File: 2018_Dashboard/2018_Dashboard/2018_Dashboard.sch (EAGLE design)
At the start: 29 parts, among them U1 SN74HC595D, U2 ATMEGA328P_PDIP_EZ, U3 SN74HC595D

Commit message: Changed resistors from before seven segment to after seven segment, reduced number of resistors
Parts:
- removed DISP1: ATA8041AB, SparkFun-LED:7-SEGMENT-4DIGIT-20MM-BLUE
- removed R5, R6, R7: 330, SparkFun-Resistors:330OHM-0603-1/10W-1%
- removed U2: ATMEGA328P_PDIP_EZ, SparkFun-IC-Microcontroller:ATMEGA328P_PDIP_EZ
- added BLUE2, BLUE3, BLUE4, LED13: TLLG4400, led:TLLG4400
- added C1: 0.1uF, SparkFun-Capacitors:0.1UF-0603-25V-(+80/-20%)
- added C2, C3: 22pF, SparkFun-Capacitors:22PF-0603-50V-5%
- added C4, C5: 560pF, SparkFun-Capacitors:560PF-0603-50V-5%
- added CAN, POWER: (no value), SparkFun-Connectors:CONN_02
- added CANH, CANL: 100, SparkFun-Resistors:100OHM-0603-1/4W-5%
- added CAN_INTERFACE: MCP2551, SparkFun-IC-Comms:MCP2551
- added CAN_SERIAL: MCP2515, SparkFun-IC-Comms:MCP2515(MCP2510)SO
- added CONTROL: ATMEGA328P_TQFP, SparkFun-IC-Microcontroller:ATMEGA328P_TQFP
- added PROGRAM: 455-1750-1-ND, SparkFun-Connectors:CONN_03
- added R17, R18, R19, R20: 330, SparkFun-Resistors:330OHM-0603-1/10W-1%
- added R21: 10k, SparkFun-Resistors:10KOHM-0603-1/10W-1%
- added R22: 4.7k, SparkFun-Resistors:4.7KOHM-0603-1/10W-1%
- added SEVEN_SEGMENT: ATA8041AB, SparkFun-LED:7-SEGMENT-4DIGIT-20MM-BLUE
- added SHIFT_3: SN74HC595D, SparkFun-IC-Logic:74HC595D
- added Y1: 16MHz, SparkFun-Clocks:CRYSTAL-16MHZPTH-HC49US
- renumbered LED1 to GREEN1, LED2 to GREEN2, LED3 to GREEN3, LED4 to GREEN4, LED5 to RED1, LED6 to RED2, LED7 to RED3, LED8 to RED4, LED9 to BLUE1, U1 to SHIFT_1, U3 to SHIF_2
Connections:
- removed net N$38: BLUE1.C, GREEN1.C, GREEN2.C, GREEN3.C, GREEN4.C, RED1.C, RED2.C, RED3.C, RED4.C, SHIFT_1.GND, SHIF_2.GND, U2.GND@1, U2.GND@2
- removed net N$7: R5.2, SHIFT_1.QE
- removed net N$8: R6.2, SHIFT_1.QF
- removed net N$9: R7.2, SHIFT_1.QG
- new net CANH: CAN.2, CANH.1, CAN_INTERFACE.CANH
- new net CANL: CAN.1, CANL.1, CAN_INTERFACE.CANL
- new net GND: BLUE1.C, BLUE2.C, BLUE3.C, BLUE4.C, C1.2, C2.1, C3.1, C4.2, C5.2, CAN_INTERFACE.VSS, CONTROL.GND@3, CONTROL.GND@5, GREEN1.C, GREEN2.C, GREEN3.C, GREEN4.C, POWER.2, R22.1, RED1.C, RED2.C, RED3.C, RED4.C, SHIFT_1.GND, SHIFT_3.GND, SHIF_2.GND
- new net N$39: R9.1, SHIF_2.QE
- new net N$40: R10.1, SHIF_2.QF
- new net N$41: R11.1, SHIF_2.QG
- new net N$42: R12.1, SHIF_2.QH
- new net N$43: R13.1, SHIFT_3.QA
- new net N$44: R14.1, SHIFT_3.QB
- new net N$45: R15.1, SHIFT_3.QC
- new net N$46: R16.1, SHIFT_3.QD
- new net N$47: R2.1, SEVEN_SEGMENT.D2
- new net N$48: R3.1, SEVEN_SEGMENT.D3
- new net N$49: R4.1, SEVEN_SEGMENT.D4
- new net N$50: LED13.A, R20.1
- new net N$51: CONTROL.PC0(ADC0), LED13.C
- new net N$52: CAN_SERIAL>NAME.CS, CONTROL.PB2(SS/OC1B)
- new net N$53: CAN_SERIAL>NAME.SI, CONTROL.PB3(MOSI/OC2)
- new net N$54: CAN_SERIAL>NAME.SO, CONTROL.PB4(MISO)
- new net N$55: CAN_SERIAL>NAME.SCK, CONTROL.PB5(SCK)
- new net N$56: CAN_SERIAL>NAME.INT, CONTROL.PD2(INT0)
- new net N$57: CAN_INTERFACE.TXD, CAN_SERIAL>NAME.TXCAN
- new net N$58: CAN_INTERFACE.RXD, CAN_SERIAL>NAME.RXCAN
- new net N$59: C3.2, CAN_SERIAL>NAME.OSC2, Y1.1
- new net N$61: CAN_INTERFACE.RS, CAN_SERIAL>NAME.RESET, PROGRAM.3, R22.2
- new net N$62: C4.1, CANH.2
- new net N$63: C2.2, CAN_SERIAL>NAME.OSC1, Y1.2
- new net N$65: C5.1, CANL.2
- new net N$67: CONTROL.PD0(RXD), PROGRAM.1
- new net N$68: CONTROL.PD1(TXD), PROGRAM.2
- new net VCC: C1.1, CAN_INTERFACE.VDD, CONTROL.AVCC, CONTROL.VCC@4, CONTROL.VCC@6, POWER.1, R20.2, R21.1, SHIFT_1.SCL, SHIFT_1.VCC, SHIFT_3.SCL, SHIFT_3.VCC, SHIF_2.SCL, SHIF_2.VCC
- net N$1: now also CONTROL.PC6(/RESET), R21.2; no longer SHIFT_1.SCL, SHIFT_1.VCC, SHIF_2.SCL, SHIF_2.VCC, U2.VCC
- net N$10: now also SHIFT_3.SER, SHIF_2.QH*; no longer DISP1.A, R1.1
- net N$11: now also SEVEN_SEGMENT.A, SHIFT_1.QA; no longer DISP1.B, R2.1
- net N$12: now also SEVEN_SEGMENT.B, SHIFT_1.QB; no longer DISP1.C, R3.1
- net N$13: now also SEVEN_SEGMENT.C, SHIFT_1.QC; no longer DISP1.D, R4.1
- net N$14: now also SEVEN_SEGMENT.D, SHIFT_1.QD; no longer DISP1.E, R5.1
- net N$15: now also SEVEN_SEGMENT.E, SHIFT_1.QE; no longer DISP1.F, R6.1
- net N$16: now also SEVEN_SEGMENT.F, SHIFT_1.QF; no longer DISP1.G, R7.1
- net N$17: now also SEVEN_SEGMENT.G, SHIFT_1.QG; no longer R8.1, SHIF_2.QA
- net N$18: now also BLUE2.A, R17.2; no longer R9.1, SHIF_2.QB
- net N$19: now also BLUE3.A, R18.2; no longer R10.1, SHIF_2.QC
- net N$20: now also CONTROL.PD5(T1); no longer U2.PD5(T1)
- net N$21: now also CONTROL.PD6(AIN0), SHIFT_3.SCK; no longer U2.PD6(AIN0)
- net N$22: now also CONTROL.PD7(AIN1), SHIFT_3.RCK; no longer U2.PD7(AIN1)
- net N$23: now also BLUE4.A, R19.2; no longer R11.1, SHIF_2.QD
- net N$24: now also R1.1, SEVEN_SEGMENT.D1; no longer R12.1, SHIF_2.QE
- net N$25: now also R19.1, SHIF_2.QA; no longer R13.1, SHIF_2.QF
- net N$26: now also R18.1, SHIF_2.QB; no longer R14.1, SHIF_2.QG
- net N$27: now also R17.1, SHIF_2.QC; no longer R15.1, SHIF_2.QH
- net N$28: now also R8.1, SHIF_2.QD; no longer R16.1, SHIF_2.QH*
- net N$3: now also SHIFT_3.QE; no longer SHIFT_1.QA
- net N$4: now also SHIFT_3.QF; no longer SHIFT_1.QB
- net N$5: now also SHIFT_3.QG; no longer SHIFT_1.QC
- net N$6: now also SHIFT_3.QH; no longer SHIFT_1.QD
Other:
- moved on the sheet: R1, R2, R3, R4

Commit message: Added silkscreen stuff
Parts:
- renumbered BLUE1 to B1, BLUE2 to B2, BLUE3 to B3, BLUE4 to B4, GREEN1 to G1, GREEN2 to G2, GREEN3 to G3, GREEN4 to G4, LED13 to OVERHEAT, RED1 to RD1, RED2 to RD2, RED3 to RD3, RED4 to RD4

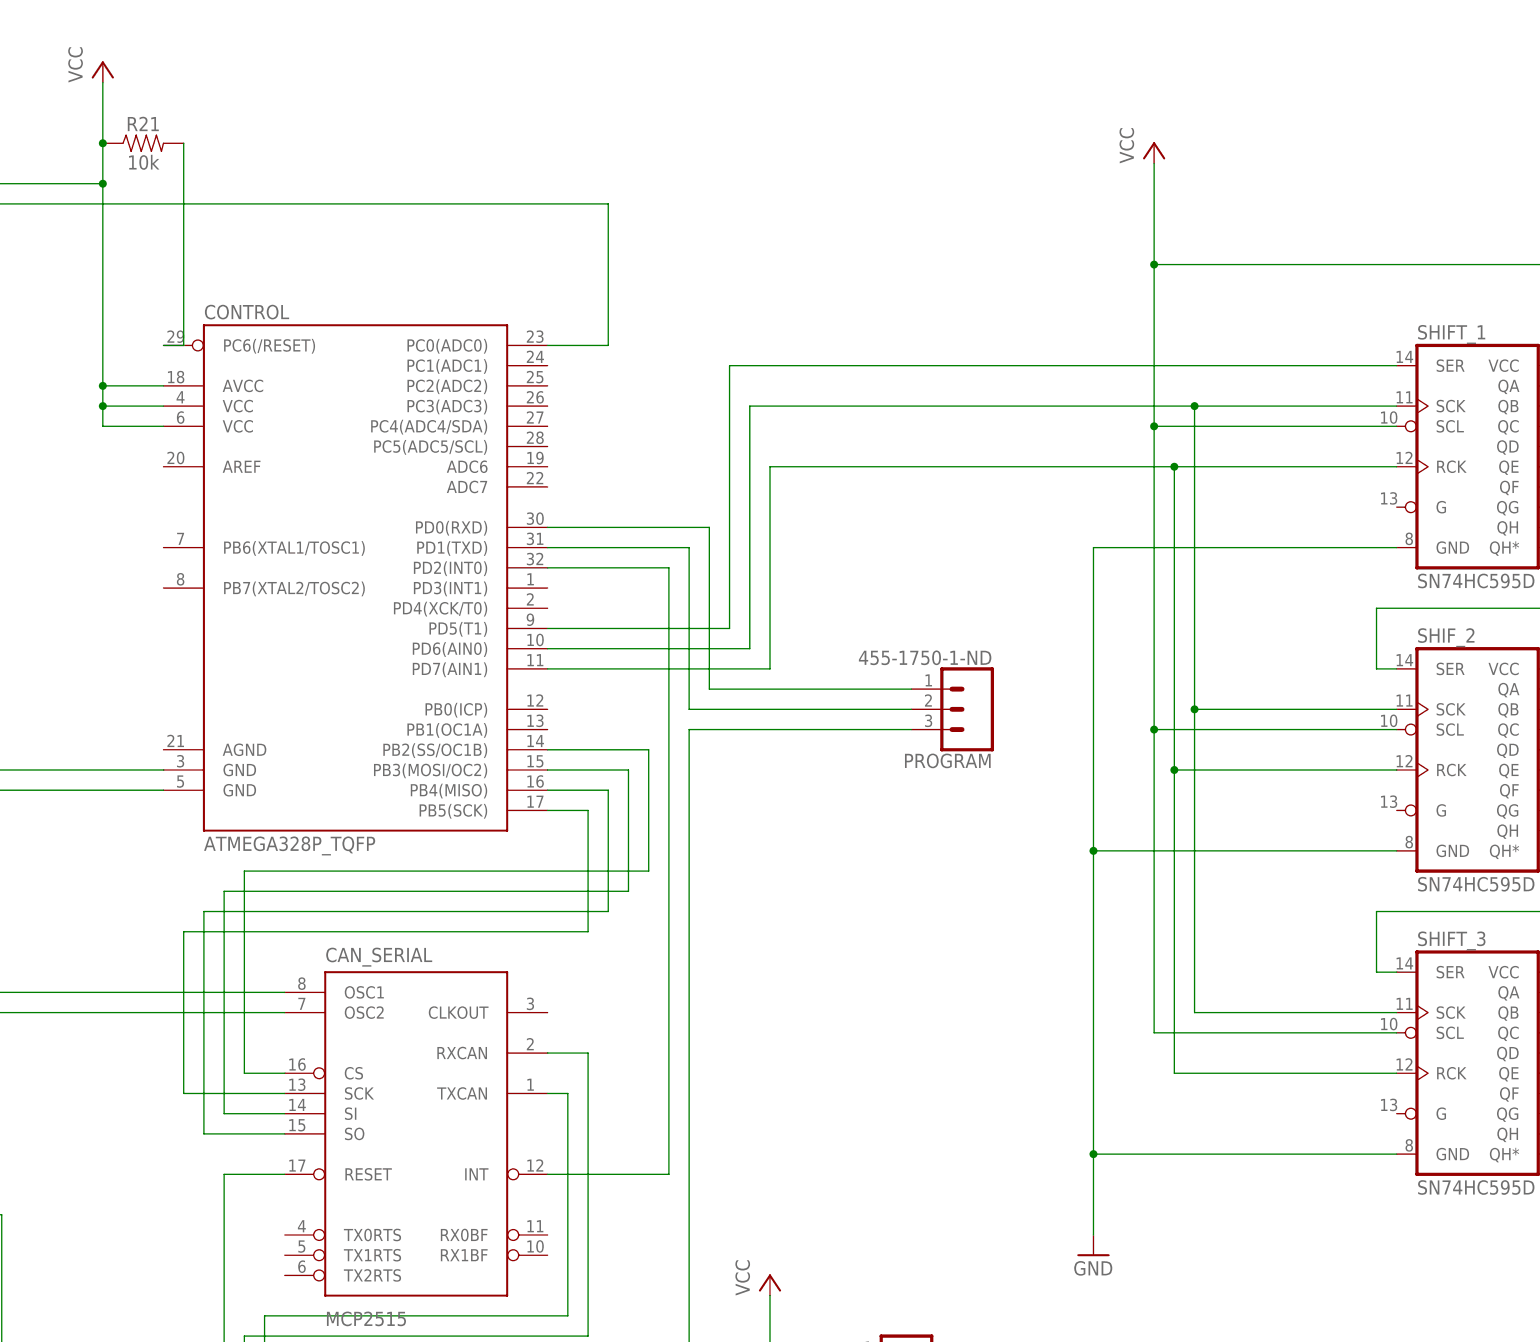
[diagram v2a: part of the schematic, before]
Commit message: fixed power net for can communication
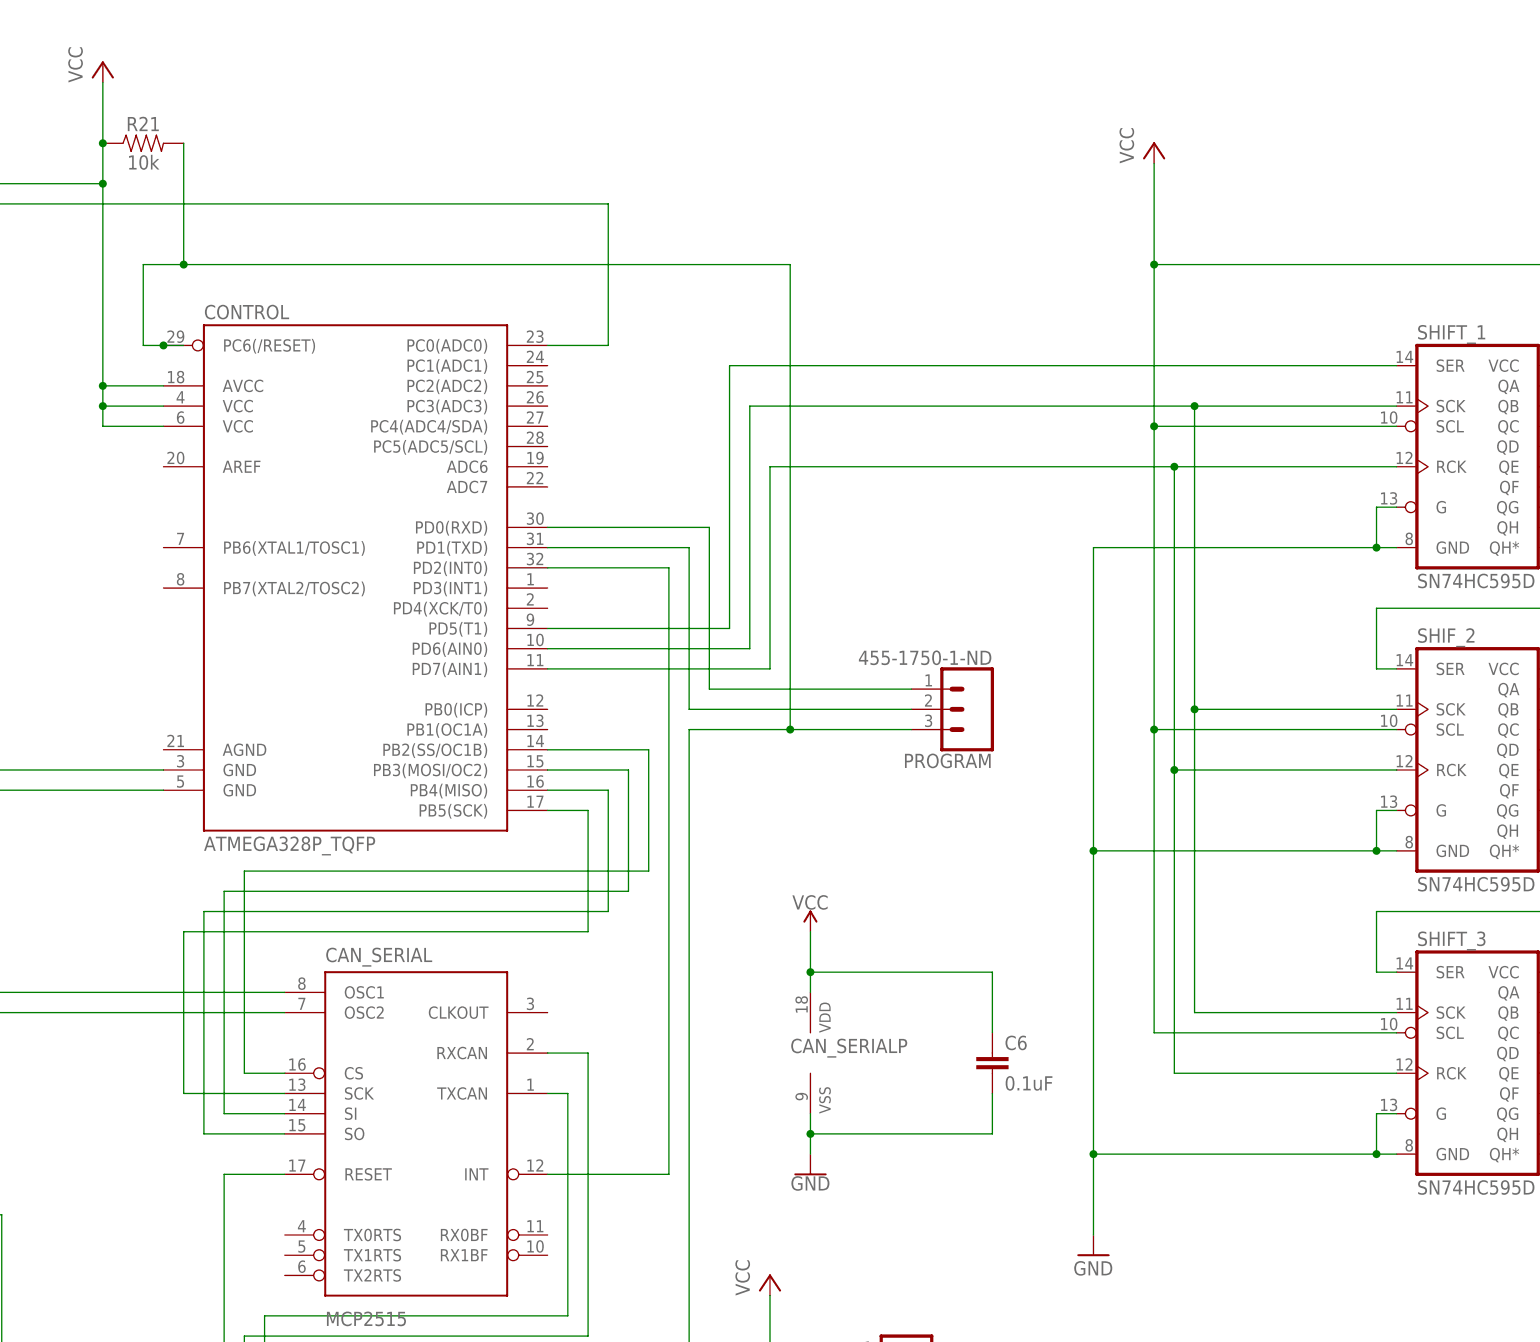
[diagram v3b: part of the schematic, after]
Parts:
- added C6: 0.1uF, SparkFun-Capacitors:0.1UF-0402-16V-10%
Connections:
- removed net N$1: CONTROL.PC6(/RESET), R21.2
- net GND: now also C6.2, CAN_SERIALP.VSS, SHIFT_1.G, SHIFT_3.G, SHIF_2.G
- net N$61: now also CONTROL.PC6(/RESET), R21.2
- net VCC: now also C6.1, CAN_SERIALP.VDD
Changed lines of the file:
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@@
 <part name="R3" library="SparkFun-Resistors" deviceset="330OHM" device="-0603-1/10W-1%" value="330"/>
 <part name="R4" library="SparkFun-Resistors" deviceset="330OHM" device="-0603-1/10W-1%" value="330"/>
+<part name="SUPPLY1" library="SparkFun-PowerSymbols" deviceset="VCC" device=""/>
+<part name="GND8" library="SparkFun-PowerSymbols" deviceset="GND" device=""/>
+<part name="C6" library="SparkFun-Capacitors" deviceset="0.1UF" device="-0402-16V-10%" value="0.1uF"/>
 </parts>
 <sheets>
@@
 <instance part="R3" gate="G$1" x="73.66" y="-50.8" rot="R90"/>
 <instance part="R4" gate="G$1" x="81.28" y="-50.8" rot="R90"/>
+<instance part="CAN_SERIAL" gate="P" x="-68.58" y="35.56"/>
+<instance part="SUPPLY1" gate="G$1" x="-68.58" y="50.8"/>
+<instance part="GND8" gate="1" x="-68.58" y="20.32"/>
+<instance part="C6" gate="G$1" x="-45.72" y="33.02"/>
 </instances>
 <busses>
@@
 <pinref part="SHIFT_3" gate="U1" pin="GND"/>
 <wire x1="-33.02" y1="12.7" x2="-33.02" y2="22.86" width="0.1524" layer="91"/>
-<wire x1="-33.02" y1="22.86" x2="5.08" y2="22.86" width="0.1524" layer="91"/>
+<wire x1="-33.02" y1="22.86" x2="2.54" y2="22.86" width="0.1524" layer="91"/>
 <pinref part="SHIF_2" gate="U1" pin="GND"/>
+<wire x1="2.54" y1="22.86" x2="5.08" y2="22.86" width="0.1524" layer="91"/>
 <wire x1="-33.02" y1="22.86" x2="-33.02" y2="60.96" width="0.1524" layer="91"/>
-<wire x1="-33.02" y1="60.96" x2="5.08" y2="60.96" width="0.1524" layer="91"/>
+<wire x1="-33.02" y1="60.96" x2="2.54" y2="60.96" width="0.1524" layer="91"/>
 <junction x="-33.02" y="22.86"/>
 <pinref part="SHIFT_1" gate="U1" pin="GND"/>
-<wire x1="5.08" y1="99.06" x2="-33.02" y2="99.06" width="0.1524" layer="91"/>
+<wire x1="2.54" y1="60.96" x2="5.08" y2="60.96" width="0.1524" layer="91"/>
+<wire x1="5.08" y1="99.06" x2="2.54" y2="99.06" width="0.1524" layer="91"/>
+<wire x1="2.54" y1="99.06" x2="-33.02" y2="99.06" width="0.1524" layer="91"/>
 <wire x1="-33.02" y1="99.06" x2="-33.02" y2="60.96" width="0.1524" layer="91"/>
 <junction x="-33.02" y="60.96"/>
+<pinref part="SHIFT_3" gate="U1" pin="G"/>
+<wire x1="5.08" y1="27.94" x2="2.54" y2="27.94" width="0.1524" layer="91"/>
+<wire x1="2.54" y1="27.94" x2="2.54" y2="22.86" width="0.1524" layer="91"/>
+<junction x="2.54" y="22.86"/>
+<pinref part="SHIF_2" gate="U1" pin="G"/>
+<wire x1="5.08" y1="66.04" x2="2.54" y2="66.04" width="0.1524" layer="91"/>
+<wire x1="2.54" y1="66.04" x2="2.54" y2="60.96" width="0.1524" layer="91"/>
+<junction x="2.54" y="60.96"/>
+<pinref part="SHIFT_1" gate="U1" pin="G"/>
+<wire x1="5.08" y1="104.14" x2="2.54" y2="104.14" width="0.1524" layer="91"/>
+<wire x1="2.54" y1="104.14" x2="2.54" y2="99.06" width="0.1524" layer="91"/>
+<junction x="2.54" y="99.06"/>
 </segment>
 <segment>
@@
 <junction x="91.44" y="-106.68"/>
 </segment>
+<segment>
+<pinref part="CAN_SERIAL" gate="P" pin="VSS"/>
+<pinref part="GND8" gate="1" pin="GND"/>
+<wire x1="-68.58" y1="27.94" x2="-68.58" y2="25.4" width="0.1524" layer="91"/>
+<pinref part="C6" gate="G$1" pin="2"/>
+<wire x1="-68.58" y1="25.4" x2="-68.58" y2="22.86" width="0.1524" layer="91"/>
+<wire x1="-45.72" y1="30.48" x2="-45.72" y2="25.4" width="0.1524" layer="91"/>
+<wire x1="-45.72" y1="25.4" x2="-68.58" y2="25.4" width="0.1524" layer="91"/>
+<junction x="-68.58" y="25.4"/>
+</segment>
 </net>
 <net name="VCC" class="0">
@@
 <wire x1="-73.66" y1="-2.54" x2="-73.66" y2="5.08" width="0.1524" layer="91"/>
 </segment>
+<segment>
+<pinref part="CAN_SERIAL" gate="P" pin="VDD"/>
+<pinref part="SUPPLY1" gate="G$1" pin="VCC"/>
+<wire x1="-68.58" y1="43.18" x2="-68.58" y2="45.72" width="0.1524" layer="91"/>
+<pinref part="C6" gate="G$1" pin="1"/>
+<wire x1="-68.58" y1="45.72" x2="-68.58" y2="50.8" width="0.1524" layer="91"/>
+<wire x1="-45.72" y1="38.1" x2="-45.72" y2="45.72" width="0.1524" layer="91"/>
+<wire x1="-45.72" y1="45.72" x2="-68.58" y2="45.72" width="0.1524" layer="91"/>
+<junction x="-68.58" y="45.72"/>
+</segment>
 </net>
 <net name="N$61" class="0">
@@
 <wire x1="-152.4" y1="-25.4" x2="-152.4" y2="-22.86" width="0.1524" layer="91"/>
 <pinref part="PROGRAM" gate="J$1" pin="3"/>
-<wire x1="-55.88" y1="76.2" x2="-83.82" y2="76.2" width="0.1524" layer="91"/>
+<wire x1="-55.88" y1="76.2" x2="-71.12" y2="76.2" width="0.1524" layer="91"/>
+<wire x1="-71.12" y1="76.2" x2="-83.82" y2="76.2" width="0.1524" layer="91"/>
 <wire x1="-83.82" y1="76.2" x2="-83.82" y2="-7.62" width="0.1524" layer="91"/>
 <wire x1="-83.82" y1="-7.62" x2="-91.44" y2="-7.62" width="0.1524" layer="91"/>
 <junction x="-91.44" y="-7.62"/>
-</segment>
-</net>
-<net name="N$1" class="0">
-<segment>
 <pinref part="R21" gate="G$1" pin="2"/>
+<wire x1="-147.32" y1="149.86" x2="-147.32" y2="134.62" width="0.1524" layer="91"/>
+<wire x1="-71.12" y1="76.2" x2="-71.12" y2="134.62" width="0.1524" layer="91"/>
+<wire x1="-71.12" y1="134.62" x2="-147.32" y2="134.62" width="0.1524" layer="91"/>
+<junction x="-71.12" y="76.2"/>
+<wire x1="-147.32" y1="134.62" x2="-152.4" y2="134.62" width="0.1524" layer="91"/>
+<junction x="-147.32" y="134.62"/>
 <pinref part="CONTROL" gate="U$1" pin="PC6(/RESET)"/>
-<wire x1="-147.32" y1="149.86" x2="-147.32" y2="124.46" width="0.1524" layer="91"/>
 <wire x1="-147.32" y1="124.46" x2="-149.86" y2="124.46" width="0.1524" layer="91"/>
+<wire x1="-152.4" y1="134.62" x2="-152.4" y2="124.46" width="0.1524" layer="91"/>
+<wire x1="-152.4" y1="124.46" x2="-149.86" y2="124.46" width="0.1524" layer="91"/>
+<junction x="-149.86" y="124.46"/>
 </segment>
 </net>
@@
 </sheet>
 </sheets>
+<errors>
+</errors>
 </schematic>
 </drawing>
